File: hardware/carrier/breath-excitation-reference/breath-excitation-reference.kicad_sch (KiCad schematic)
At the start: 13 parts

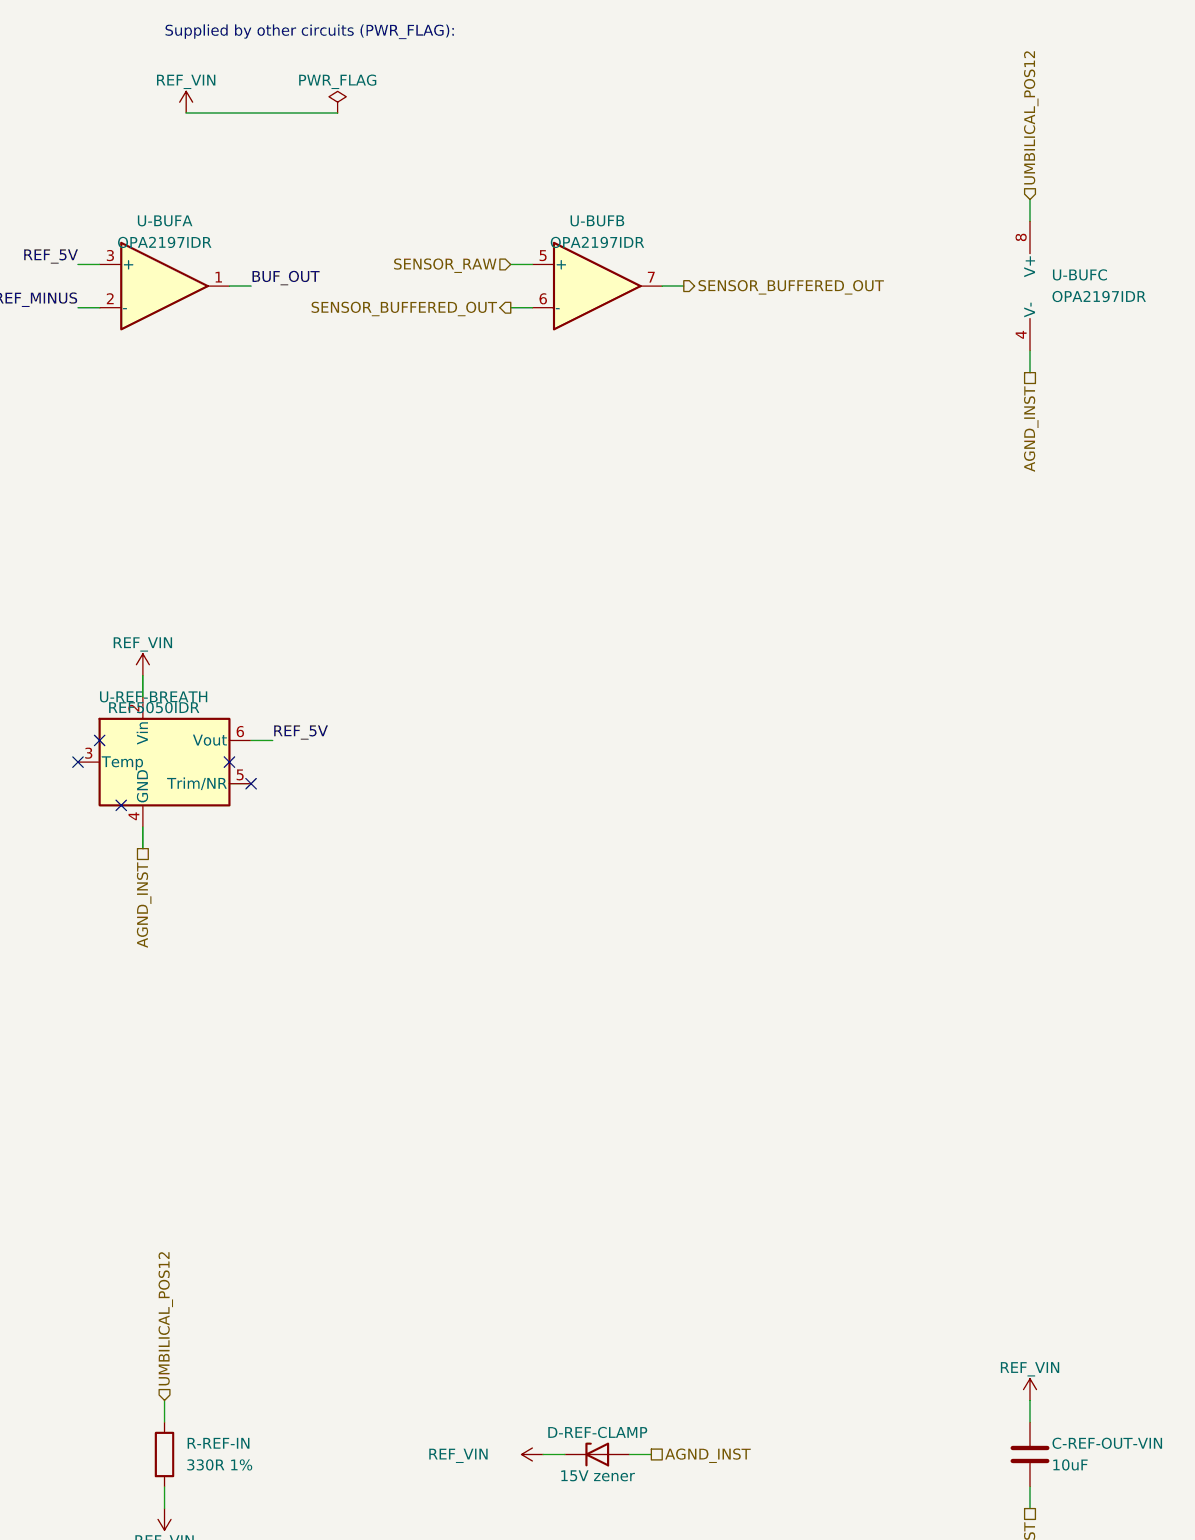
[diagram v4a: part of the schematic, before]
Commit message: Instrument power entry: Q-INRUSH soft start between the connector and the bulk (sheets, WIP)
Q-INRUSH (AO3401A) and its gate network on the power-entry-instrument sheet;
the switched side is INST_POS12, which the LED drive and the analog reference
now receive. Exported; main board ERC clean. BOM, nets, sims and pages follow.

Co-Authored-By: Claude Opus 5.5 <noreply@anthropic.com>
Claude-Session: https://claude.ai/code/session_01LmB4muFXnoLprWX4JzuJ5A
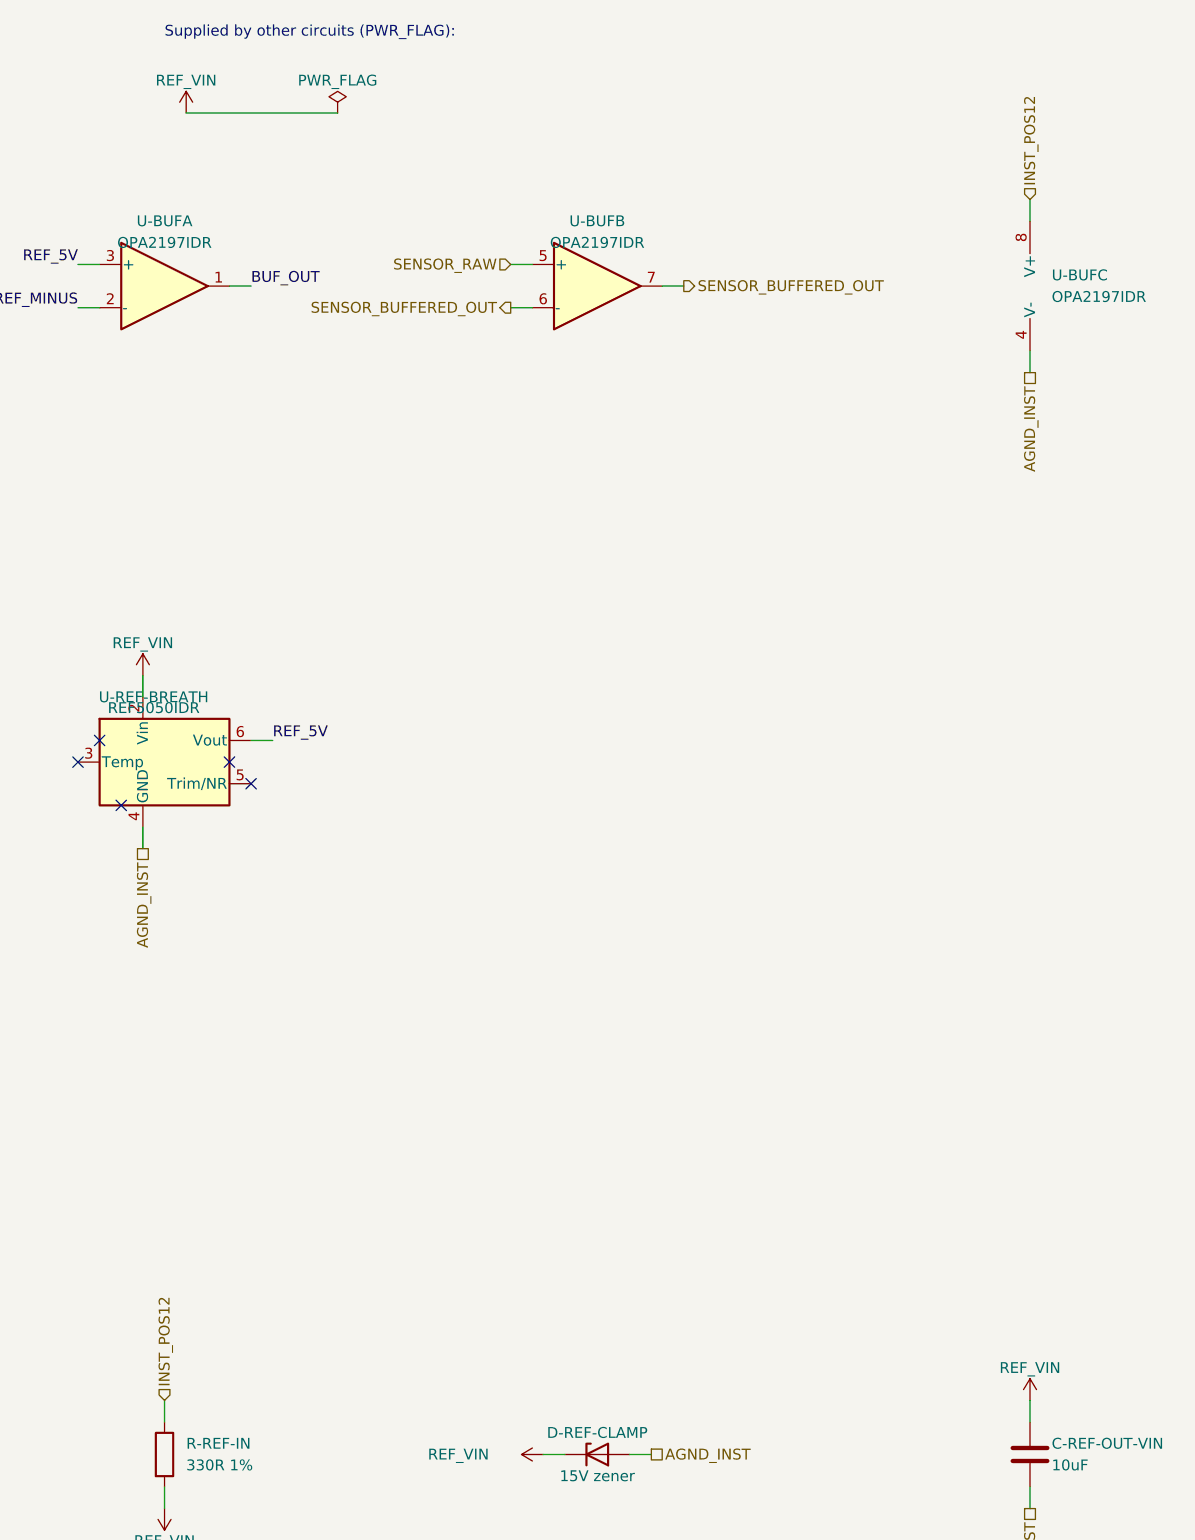
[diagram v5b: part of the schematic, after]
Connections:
- net UMBILICAL_POS12 renamed INST_POS12
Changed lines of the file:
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@@
   )
   (wire (pts (xy 40.64 184.15) (xy 40.64 181.61)) (stroke (width 0) (type default)))
-  (hierarchical_label "UMBILICAL_POS12" (shape input) (at 40.64 181.61 90) (effects (font (size 1.27 1.27)) (justify left))
+  (hierarchical_label "INST_POS12" (shape input) (at 40.64 181.61 90) (effects (font (size 1.27 1.27)) (justify left))
     (property "Dir" "in" (at 40.64 181.61 0) (effects (font (size 1.27 1.27)) hide))
-    (property "From" "module/umbilical-load-switch" (at 40.64 181.61 0) (effects (font (size 1.27 1.27)) hide)))
+    (property "From" "carrier/power-entry-instrument" (at 40.64 181.61 0) (effects (font (size 1.27 1.27)) hide)))
   (wire (pts (xy 142.24 43.18) (xy 142.24 40.64)) (stroke (width 0) (type default)))
-  (hierarchical_label "UMBILICAL_POS12" (shape input) (at 142.24 40.64 90) (effects (font (size 1.27 1.27)) (justify left))
+  (hierarchical_label "INST_POS12" (shape input) (at 142.24 40.64 90) (effects (font (size 1.27 1.27)) (justify left))
     (property "Dir" "in" (at 142.24 40.64 0) (effects (font (size 1.27 1.27)) hide))
-    (property "From" "module/umbilical-load-switch" (at 142.24 40.64 0) (effects (font (size 1.27 1.27)) hide)))
+    (property "From" "carrier/power-entry-instrument" (at 142.24 40.64 0) (effects (font (size 1.27 1.27)) hide)))
   (wire (pts (xy 40.64 191.77) (xy 40.64 194.31)) (stroke (width 0) (type default)))
   (symbol (lib_id "power:+12V") (at 40.64 194.31 180) (unit 1)

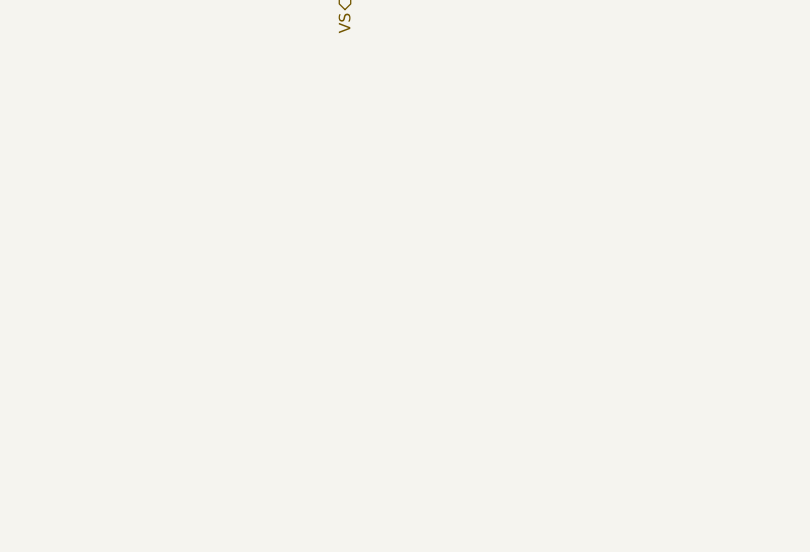
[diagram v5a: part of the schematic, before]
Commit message: Sensor Figure 3 capacitors and U-BUF bypass drawn; VS load simulated as built; F1 verification ledger
C-SENSOR-VS-BULK/-HF and C-SENSOR-OUT at U-BREATH (owner, A1-5), C-DEC-BUF at
U-BUF V+ (A8-1); excitation sims load VS with everything netlisted there.
VERIFIED-F1.md closes every A1 id and A8-1/A8-4, with A1-1's options for the owner.

Co-Authored-By: Claude Opus 5.5 <noreply@anthropic.com>
Claude-Session: https://claude.ai/code/session_01LmB4muFXnoLprWX4JzuJ5A
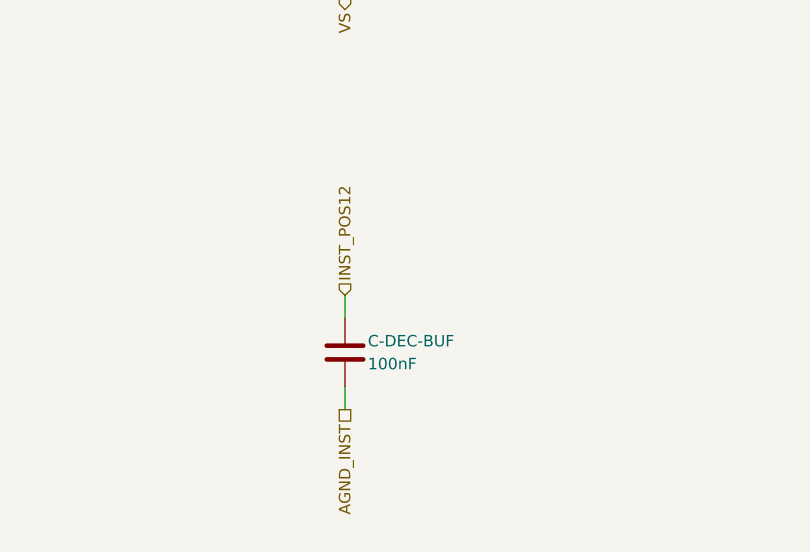
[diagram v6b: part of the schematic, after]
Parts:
- added C-DEC-BUF: 100nF, Capacitor_SMD:C_0805_2012Metric, symbol Device:C
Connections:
- net AGND_INST: now also C-DEC-BUF.2
- net INST_POS12: now also C-DEC-BUF.1
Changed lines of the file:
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@@
   )
   (text "FROM THE HAND-WRITTEN NETLIST THIS SHEET REPLACES (verbatim; the part notes are on each part's Note field):\n\nAUTHORITATIVE for connectivity. THE DRAWING IS ON ANOTHER PAGE - carrier.md §2, which draws the reference, the\nbuffer, the sensor and the ADC in one picture because they are one signal path. This circuit owns the\nreference and both halves of the OPA2197; carrier/breath-adc and interfaces/breath-sense-link own the rest and\nnetlist it against the same drawing.\n\nTHE REFERENCE'S INPUT IS PROTECTED, AND THE TVS ON THE RAIL DOES NOT DO IT. The REF5050's input is 18 V\nabsolute maximum [ds REF5050.pdf p.5], and the rail's SMAJ15A only starts to break down at 16.7-18.5 V and\nclamps at 24.4 V [ds LITTELFUSE-SMAJ-SERIES-SMAJ15A.pdf p.2]. So the reference has its own: R-REF-IN in\nseries, D-REF-CLAMP to the star behind it. 1.2 mA at most [ds p.8] drops 0.4 V; at the SMAJ's clamp the zener\ntakes (24.4 - 15.75) / 330 = 26 mA, and holds the input under 18 V for the 10/1000 us surge the SMAJ is rated\nat - an RC alone would not, its time constant being shorter.\n\nONE PACKAGE, TWO JOBS: half A buffers the 5.000 V into the sensor, half B the sensor's output before anything\nloads it. Single supply from +12 V, V- on the analog star.\n\nThe REF5050's other pins [ds datasheets/analog/REF5050.pdf Table 5-1]: TEMP, TRIM/NR and NC are left open -\nthe trim and the noise-reduction capacitor are not used; DNC must not be connected." (at 256.54 38.099999999999994 0) (effects (font (size 1.27 1.27)) (justify left top)))
+  (symbol (lib_id "Device:C") (at 193.04 279.4 0) (unit 1)
+    (in_bom yes) (on_board yes) (dnp no)
+    (property "Reference" "C-DEC-BUF" (at 195.57999999999998 278.13 0) (effects (font (size 1.27 1.27)) (justify left)))
+    (property "Value" "100nF" (at 195.57999999999998 280.66999999999996 0) (effects (font (size 1.27 1.27)) (justify left)))
+    (property "Footprint" "Capacitor_SMD:C_0805_2012Metric" (at 193.04 279.4 0) (effects (font (size 1.27 1.27)) hide))
+    (property "Datasheet" "" (at 193.04 279.4 0) (effects (font (size 1.27 1.27)) hide))
+    (property "Row" "C-DECOUPLE-CARRIER" (at 193.04 279.4 0) (effects (font (size 1.27 1.27)) hide))
+    (property "Pins" "1=1 2=2" (at 193.04 279.4 0) (effects (font (size 1.27 1.27)) hide))
+    (property "Note" "U-BUF's +12 V supply pin to the analog star, at the pin: the op-amp's own bypass, which the LED row's decouplers on the same net are not (A8-1, 2026-10-01)" (at 193.04 279.4 0) (effects (font (size 1.27 1.27)) hide))
+    (property "Manufacturer" "YAGEO" (at 193.04 279.4 0) (effects (font (size 1.27 1.27)) hide))
+    (property "MPN" "CC0805KRX7R9BB104" (at 193.04 279.4 0) (effects (font (size 1.27 1.27)) hide))
+    (property "LCSC" "C49678" (at 193.04 279.4 0) (effects (font (size 1.27 1.27)) hide))
+    (property "Assembly" "machine" (at 193.04 279.4 0) (effects (font (size 1.27 1.27)) hide))
+    (pin "1")
+    (pin "2")
+    (instances (project "main-board" (path "/b12a49ac-ffa0-5078-b2ba-e15d161f1936/6d52cf50-898d-5f10-a456-90ce50679c12" (reference "C204") (unit 1))) (project "breath-excitation-reference" (path "/5307c492-2437-5eeb-8e77-9d437de128d5" (reference "C-DEC-BUF") (unit 1))))
+  )
+  (wire (pts (xy 193.04 275.59) (xy 193.04 273.05)) (stroke (width 0) (type default)))
+  (hierarchical_label "INST_POS12" (shape input) (at 193.04 273.05 90) (effects (font (size 1.27 1.27)) (justify left))
+    (property "Dir" "in" (at 193.04 273.05 0) (effects (font (size 1.27 1.27)) hide))
+    (property "From" "carrier/power-entry-instrument" (at 193.04 273.05 0) (effects (font (size 1.27 1.27)) hide)))
+  (wire (pts (xy 193.04 283.21) (xy 193.04 285.75)) (stroke (width 0) (type default)))
+  (hierarchical_label "AGND_INST" (shape passive) (at 193.04 285.75 270) (effects (font (size 1.27 1.27)) (justify right))
+    (property "Dir" "ref" (at 193.04 285.75 0) (effects (font (size 1.27 1.27)) hide))
+    (property "From" "carrier/power-entry-instrument" (at 193.04 285.75 0) (effects (font (size 1.27 1.27)) hide)))
   (sheet_instances (path "/" (page "1")))
 )
